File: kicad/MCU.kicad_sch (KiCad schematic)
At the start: 78 parts, among them J3 USART, J4 FAN, J5 USB_A, J6 Display, Q6 2N7002NXAK, Q7 2N7002K, Q8 2N7002K, SW1 ENC0 (Voltage), SW2 ENC1 (Current), SW3 BOOT, SW4 RST, U4 USBLC6-2SC6, U5 MCP9700A, U6 STM32F373C8Tx, Y1 Crystal

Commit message: Removed unnecessary stuff on fan tacho output
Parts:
- removed D7: SS16HE, Diode_SMD:D_SOD-323_HandSoldering, symbol Device:D_Schottky
- removed R30, R31, R35, R38: 10K, Resistor_SMD:R_0805_2012Metric_Pad1.20x1.40mm_HandSolder, symbol Device:R
- added C43: 100nF, symbol Device:C_Small
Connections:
- net GND: now also C43.2
- net at J4.3 (Pin_3), R34.2: now also C43.1
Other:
- moved on the sheet: R34

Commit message: Schematic work
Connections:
- net Iread: no longer U6.18 (PB0)
- net Iset: now also U6.16 (PA6); no longer U6.15 (PA5)
- net TEMP: now also U6.28 (PD8); no longer U6.14 (PA4)
- net Vread: no longer U6.19 (PB1)
- net Vset: now also U6.14 (PA4); no longer U6.16 (PA6)
- no-connect marks 8 -> 10

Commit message: Bunch of stuff
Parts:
- C42, C43: footprint (none) -> Capacitor_SMD:C_0805_2012Metric_Pad1.18x1.45mm_HandSolder
- J3: footprint (none) -> Connector_PinHeader_2.54mm:PinHeader_1x04_P2.54mm_Vertical
- JP1: value Jumper_2_Open -> 3V3 pullup on usb line; footprint (none) -> Jumper:SolderJumper-2_P1.3mm_Open_Pad1.0x1.5mm
- NT2, NT3, NT4, NT5: footprint (none) -> NetTie:NetTie-2_SMD_Pad0.5mm
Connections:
- net GNDA is gone; now on net GND: C18.1, C19.1, C20.1, C22.1, C23.1, C24.1, C28.1, C29.1, C30.1, U6.23 (VSSSD), U6.8 (VSSA)
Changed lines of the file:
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@@
 	)
 	(junction
+		(at 166.37 111.76)
+		(diameter 0)
+		(color 0 0 0 0)
+	)
+	(junction
 		(at 26.67 68.58)
 		(diameter 0)
@@
 	)
 	(junction
-		(at 171.45 111.76)
-		(diameter 0)
-		(color 0 0 0 0)
-	)
-	(junction
 		(at 26.67 26.67)
 		(diameter 0)
@@
 	)
 	(junction
+		(at 168.91 111.76)
+		(diameter 0)
+		(color 0 0 0 0)
+	)
+	(junction
 		(at 16.51 43.18)
 		(diameter 0)
@@
 	(wire
 		(pts
+			(xy 166.37 111.76) (xy 168.91 111.76)
+		)
+		(stroke
+			(width 0)
+			(type default)
+		)
+	)
+	(wire
+		(pts
 			(xy 158.75 134.62) (xy 163.83 134.62)
 		)
@@
 	(wire
 		(pts
-			(xy 171.45 111.76) (xy 173.99 111.76)
-		)
-		(stroke
-			(width 0)
-			(type default)
-		)
-	)
-	(wire
-		(pts
 			(xy 162.56 163.83) (xy 153.67 163.83)
 		)
@@
 	(wire
 		(pts
-			(xy 173.99 111.76) (xy 173.99 114.3)
-		)
-		(stroke
-			(width 0)
-			(type default)
-		)
-	)
-	(wire
-		(pts
 			(xy 166.37 27.94) (xy 168.91 27.94)
 		)
@@
 			)
 		)
-		(property "Footprint" ""
+		(property "Footprint" "Capacitor_SMD:C_0805_2012Metric_Pad1.18x1.45mm_HandSolder"
 			(at 158.75 138.43 0)
 			(effects
@@
 	)
 	(symbol
-		(lib_id "power:GNDA")
-		(at 173.99 114.3 0)
-		(unit 1)
-		(exclude_from_sim no)
-		(in_bom yes)
-		(on_board yes)
-		(dnp no)
-		(property "Reference" "#PWR068"
-			(at 173.99 120.65 0)
-			(effects
-				(font
-					(size 1.27 1.27)
-				)
-				(hide yes)
-			)
-		)
-		(property "Value" "GNDA"
-			(at 174.117 118.6942 0)
-			(effects
-				(font
-					(size 1.27 1.27)
-				)
-			)
-		)
-		(property "Footprint" ""
-			(at 173.99 114.3 0)
-			(effects
-				(font
-					(size 1.27 1.27)
-				)
-				(hide yes)
-			)
-		)
-		(property "Datasheet" ""
-			(at 173.99 114.3 0)
-			(effects
-				(font
-					(size 1.27 1.27)
-				)
-				(hide yes)
-			)
-		)
-		(property "Description" "Power symbol creates a global label with name \"GNDA\" , analog ground"
-			(at 173.99 114.3 0)
-			(effects
-				(font
-					(size 1.27 1.27)
-				)
-				(hide yes)
-			)
-		)
-		(pin "1"
-		)
-		(instances
-			(project ""
-				(path "/9538e4ed-27e6-4c37-b989-9859dc0d49e8/00000000-0000-0000-0000-00005f1751cc"
-					(reference "#PWR068")
-					(unit 1)
-				)
-			)
-		)
-	)
-	(symbol
 		(lib_id "Switch:SW_Push")
 		(at 113.03 40.64 0)
@@
 			)
 		)
-		(property "Value" "GNDA"
+		(property "Value" "GND"
 			(at 16.637 64.0842 0)
 			(effects
@@
 			)
 		)
-		(property "Value" "GNDA"
+		(property "Value" "GND"
 			(at 16.637 47.5742 0)
 			(effects
@@
 			)
 		)
-		(property "Value" "GNDA"
+		(property "Value" "GND"
 			(at 16.637 31.0642 0)
 			(effects
@@
 			)
 		)
-		(property "Footprint" ""
+		(property "Footprint" "Connector_PinHeader_2.54mm:PinHeader_1x04_P2.54mm_Vertical"
 			(at 29.21 90.17 0)
 			(effects
@@
 			)
 		)
-		(property "Value" "Jumper_2_Open"
+		(property "Value" "3V3 pullup on usb line"
 			(at 91.44 95.25 0)
 			(effects
@@
 			)
 		)
-		(property "Footprint" ""
+		(property "Footprint" "Jumper:SolderJumper-2_P1.3mm_Open_Pad1.0x1.5mm"
 			(at 91.44 99.06 0)
 			(effects
@@
 			)
 		)
-		(property "Footprint" ""
+		(property "Footprint" "NetTie:NetTie-2_SMD_Pad0.5mm"
 			(at 60.96 68.58 0)
 			(effects
@@
 			)
 		)
-		(property "Footprint" ""
+		(property "Footprint" "NetTie:NetTie-2_SMD_Pad0.5mm"
 			(at 52.07 21.59 0)
 			(effects
@@
 			)
 		)
-		(property "Footprint" ""
+		(property "Footprint" "NetTie:NetTie-2_SMD_Pad0.5mm"
 			(at 48.26 54.61 0)
 			(effects
@@
 			)
 		)
-		(property "Footprint" ""
+		(property "Footprint" "Capacitor_SMD:C_0805_2012Metric_Pad1.18x1.45mm_HandSolder"
 			(at 33.02 134.62 0)
 			(effects
@@
 			)
 		)
-		(property "Footprint" ""
+		(property "Footprint" "NetTie:NetTie-2_SMD_Pad0.5mm"
 			(at 52.07 38.1 0)
 			(effects

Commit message: Minor changes
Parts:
- removed C42: ?, Capacitor_SMD:C_0805_2012Metric_Pad1.18x1.45mm_HandSolder, symbol Device:C_Small
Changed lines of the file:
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@@
 	)
 	(junction
-		(at 158.75 134.62)
-		(diameter 0)
-		(color 0 0 0 0)
-	)
-	(junction
 		(at 26.67 59.69)
 		(diameter 0)
@@
 	(wire
 		(pts
-			(xy 158.75 142.24) (xy 158.75 140.97)
-		)
-		(stroke
-			(width 0)
-			(type default)
-		)
-	)
-	(wire
-		(pts
 			(xy 31.75 162.56) (xy 31.75 161.29)
 		)
@@
 	(wire
 		(pts
-			(xy 158.75 134.62) (xy 163.83 134.62)
+			(xy 156.21 134.62) (xy 163.83 134.62)
 		)
 		(stroke
@@
 	(wire
 		(pts
-			(xy 156.21 134.62) (xy 158.75 134.62)
-		)
-		(stroke
-			(width 0)
-			(type default)
-		)
-	)
-	(wire
-		(pts
 			(xy 162.56 163.83) (xy 153.67 163.83)
 		)
@@
 	(wire
 		(pts
-			(xy 158.75 134.62) (xy 158.75 135.89)
-		)
-		(stroke
-			(width 0)
-			(type default)
-		)
-	)
-	(wire
-		(pts
 			(xy 41.91 129.54) (xy 41.91 140.97)
 		)
@@
 	(wire
 		(pts
-			(xy 146.05 142.24) (xy 158.75 142.24)
-		)
-		(stroke
-			(width 0)
-			(type default)
-		)
-	)
-	(wire
-		(pts
 			(xy 115.57 179.07) (xy 120.65 179.07)
 		)
@@
 					(unit 1)
 				)
-			)
-		)
-	)
-	(symbol
-		(lib_id "Device:C_Small")
-		(at 158.75 138.43 0)
-		(unit 1)
-		(exclude_from_sim no)
-		(in_bom yes)
-		(on_board yes)
-		(dnp no)
-		(property "Reference" "C42"
-			(at 161.0868 137.2616 0)
-			(effects
-				(font
-					(size 1.27 1.27)
-				)
-				(justify left)
-			)
-		)
-		(property "Value" "?"
-			(at 161.0868 139.573 0)
-			(effects
-				(font
-					(size 1.27 1.27)
-				)
-				(justify left)
-			)
-		)
-		(property "Footprint" "Capacitor_SMD:C_0805_2012Metric_Pad1.18x1.45mm_HandSolder"
-			(at 158.75 138.43 0)
-			(effects
-				(font
-					(size 1.27 1.27)
-				)
-				(hide yes)
-			)
-		)
-		(property "Datasheet" "~"
-			(at 158.75 138.43 0)
-			(effects
-				(font
-					(size 1.27 1.27)
-				)
-				(hide yes)
-			)
-		)
-		(property "Description" "Unpolarized capacitor, small symbol"
-			(at 158.75 138.43 0)
-			(effects
-				(font
-					(size 1.27 1.27)
-				)
-				(hide yes)
-			)
-		)
-		(pin "1"
-		)
-		(pin "2"
-		)
-		(instances
-			(project ""
-				(path "/9538e4ed-27e6-4c37-b989-9859dc0d49e8/00000000-0000-0000-0000-00005f1751cc"
-					(reference "C42")
-					(unit 1)
-				)

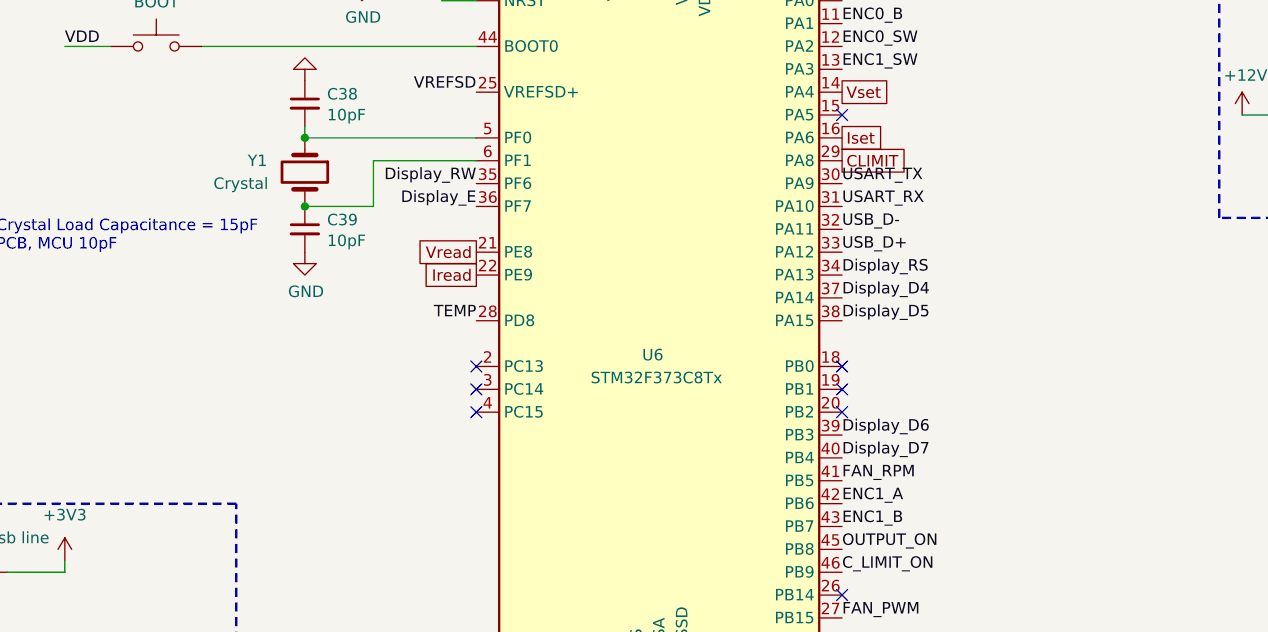
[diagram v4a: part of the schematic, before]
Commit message: Added series termination on display lines
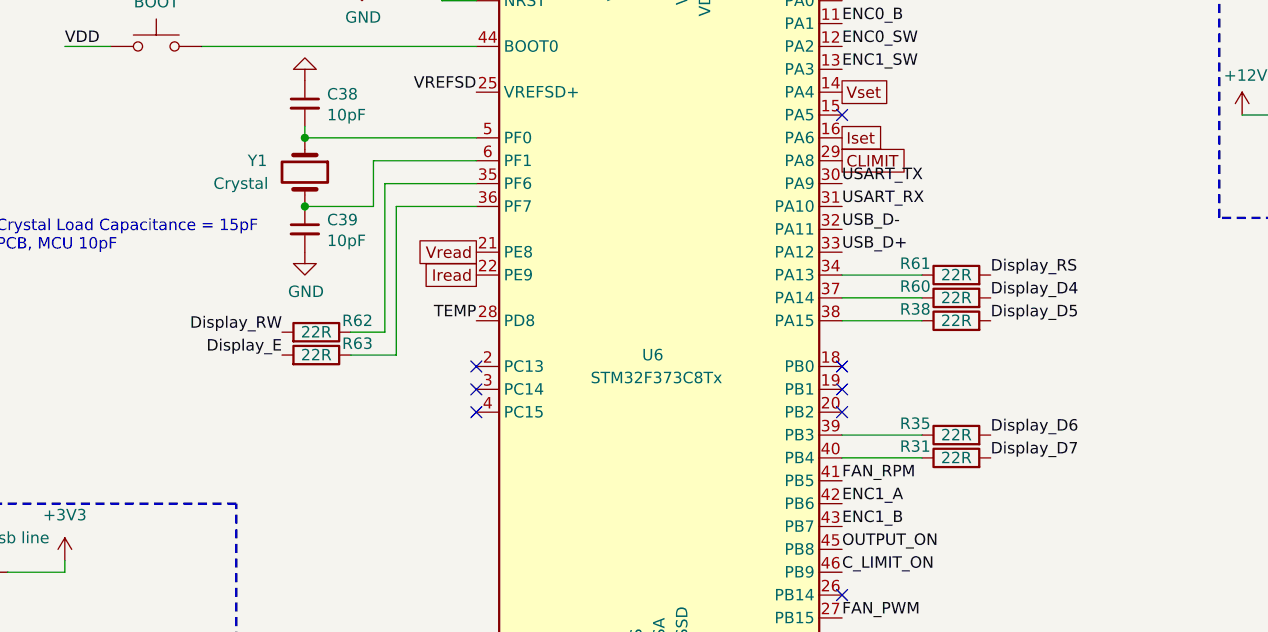
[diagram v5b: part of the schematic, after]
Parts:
- added R31, R35, R38, R60, R61, R62, R63: 22R, Resistor_SMD:R_0805_2012Metric_Pad1.20x1.40mm_HandSolder, symbol Device:R
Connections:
- net Display_D4: now also R60.2; no longer U6.37 (PA14)
- net Display_D5: now also R38.2; no longer U6.38 (PA15)
- net Display_D6: now also R35.2; no longer U6.39 (PB3)
- net Display_D7: now also R31.2; no longer U6.40 (PB4)
- net Display_E: now also R63.2; no longer U6.36 (PF7)
- net Display_RS: now also R61.2; no longer U6.34 (PA13)
- net Display_RW: now also R62.2; no longer U6.35 (PF6)
- new net: R61.1, U6.34 (PA13)
- new net: R62.1, U6.35 (PF6)
- new net: R63.1, U6.36 (PF7)
- new net: R60.1, U6.37 (PA14)
- new net: R38.1, U6.38 (PA15)
- new net: R35.1, U6.39 (PB3)
- new net: R31.1, U6.40 (PB4)

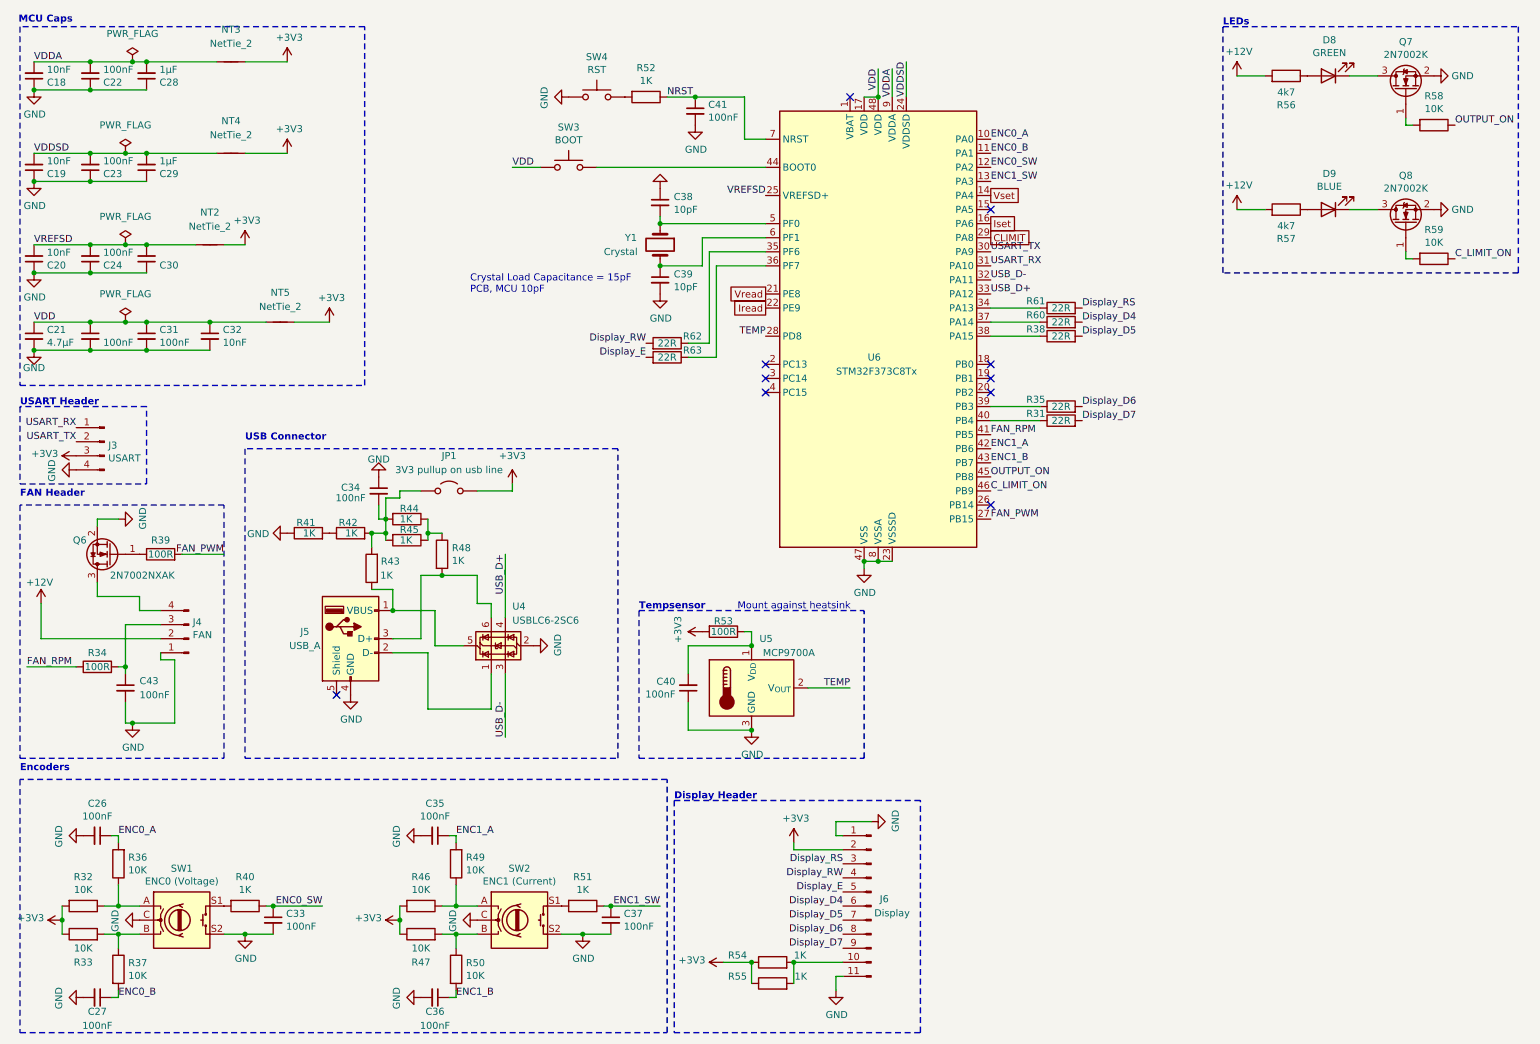
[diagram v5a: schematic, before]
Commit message: Changes and added Buck converter for 3V3
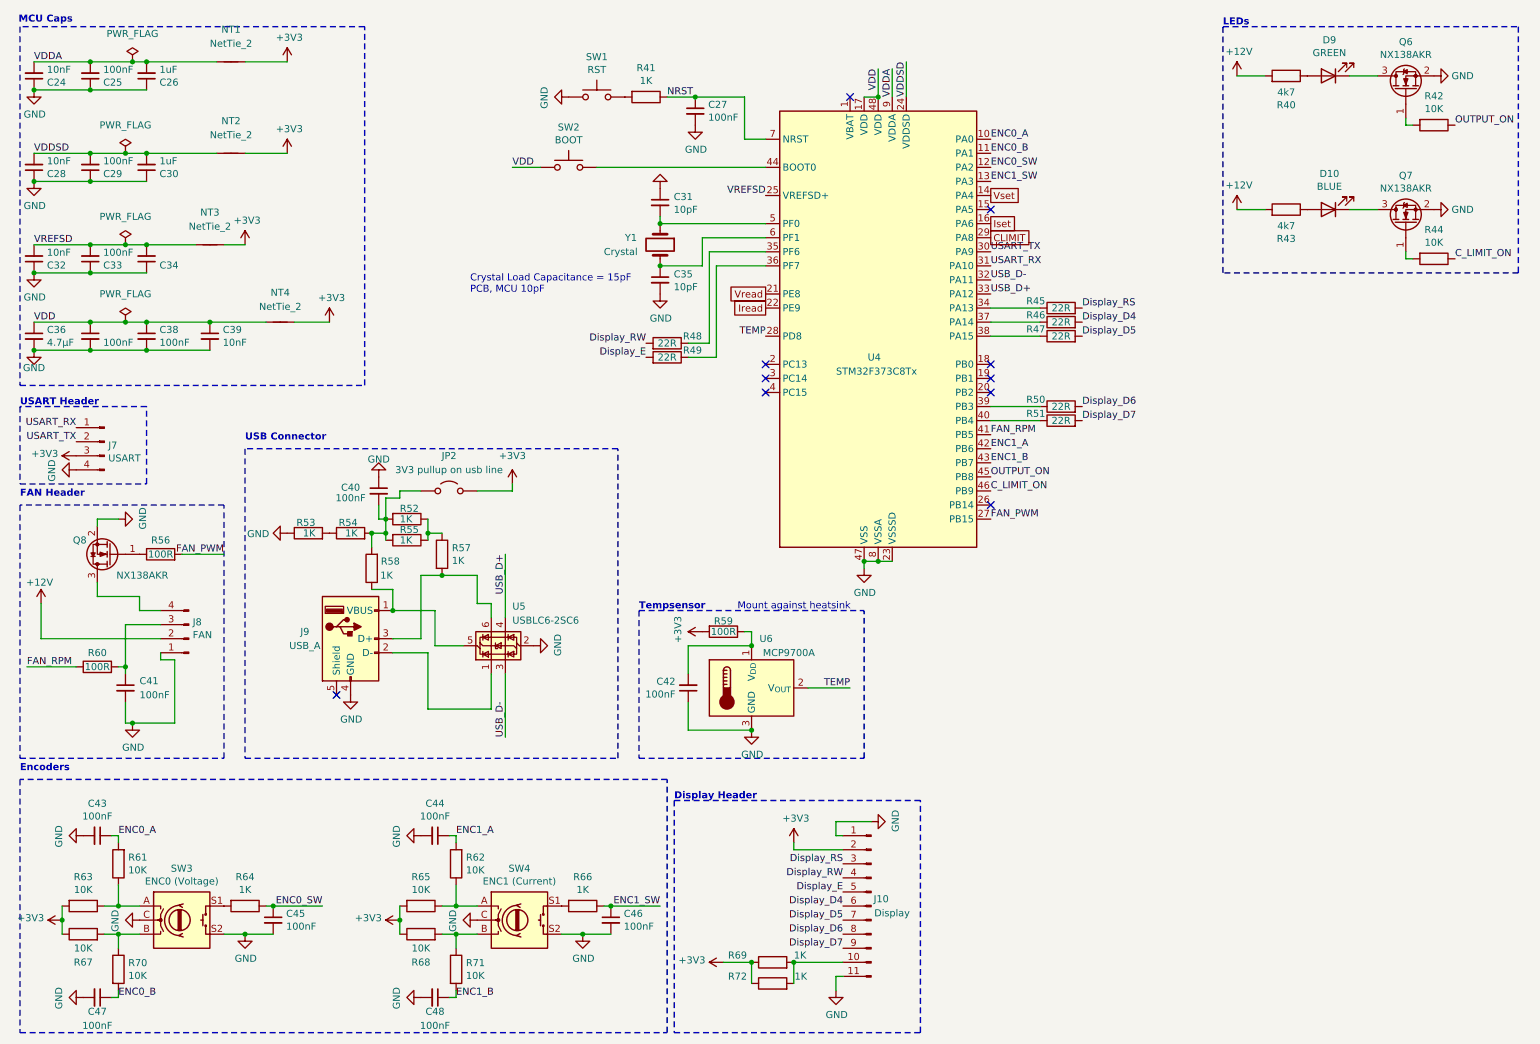
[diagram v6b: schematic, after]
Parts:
- C26: renamed from C28; value 1µF -> 1uF
- C27: renamed from C41; MPN CC0805KRX7R0BB103 -> CC0805KRX7R9BB104
- C30: renamed from C29; value 1µF -> 1uF
- C34: renamed from C30; value 1µF -> 1uF
- C36: renamed from C21; MPN GRM21BR71C475KE51L -> GRM21BR61H475ME51L
- C40: renamed from C34; MPN CC0805KRX7R0BB103 -> CC0805KRX7R9BB104
- C41: renamed from C43; MPN (none) -> CC0805KRX7R9BB104
- C42: renamed from C40; MPN CC0805KRX7R0BB103 -> CC0805KRX7R9BB104
- C43: renamed from C26; MPN CC0805KRX7R0BB103 -> CC0805KRX7R9BB104
- C44: renamed from C35; MPN CC0805KRX7R0BB103 -> CC0805KRX7R9BB104
- C45: renamed from C33; MPN CC0805KRX7R0BB103 -> CC0805KRX7R9BB104
- C46: renamed from C37; MPN CC0805KRX7R0BB103 -> CC0805KRX7R9BB104
- C47: renamed from C27; MPN CC0805KRX7R0BB103 -> CC0805KRX7R9BB104
- C48: renamed from C36; MPN CC0805KRX7R0BB103 -> CC0805KRX7R9BB104
- Q6: renamed from Q7; value 2N7002K -> NX138AKR; footprint Package_TO_SOT_SMD:SOT-23 -> Package_TO_SOT_SMD:SOT-23-3; MPN (none) -> NX138AKR
- Q7: renamed from Q8; value 2N7002K -> NX138AKR; footprint Package_TO_SOT_SMD:SOT-23 -> Package_TO_SOT_SMD:SOT-23-3; MPN (none) -> NX138AKR
- Q8: renamed from Q6; value 2N7002NXAK -> NX138AKR; footprint Package_TO_SOT_SMD:SOT-23 -> Package_TO_SOT_SMD:SOT-23-3; MPN 2N7002NXAK -> NX138AKR
- R42: renamed from R58; MPN CRCW080510K0FKEAC -> RC0805FR-1310KL
- R44: renamed from R59; MPN CRCW080510K0FKEAC -> RC0805FR-1310KL
- R61: renamed from R36; MPN CRCW080510K0FKEAC -> RC0805FR-1310KL
- R62: renamed from R49; MPN CRCW080510K0FKEAC -> RC0805FR-1310KL
- R63: renamed from R32; MPN CRCW080510K0FKEAC -> RC0805FR-1310KL
- R65: renamed from R46; MPN CRCW080510K0FKEAC -> RC0805FR-1310KL
- R67: renamed from R33; MPN CRCW080510K0FKEAC -> RC0805FR-1310KL
- R68: renamed from R47; MPN CRCW080510K0FKEAC -> RC0805FR-1310KL
- R70: renamed from R37; MPN CRCW080510K0FKEAC -> RC0805FR-1310KL
- R71: renamed from R50; MPN CRCW080510K0FKEAC -> RC0805FR-1310KL
- U4: renamed from U6; MPN (none) -> STM32F373C8Tx
- renumbered C18 to C24, C22 to C25, C19 to C28, C23 to C29, C38 to C31, C20 to C32, C24 to C33, C39 to C35, C25 to C37, C31 to C38, C32 to C39, D9 to D10, D8 to D9, J6 to J10, J3 to J7, J4 to J8, J5 to J9, JP1 to JP2, NT3 to NT1, NT4 to NT2, NT2 to NT3, NT5 to NT4, R56 to R40, R52 to R41, R57 to R43, R61 to R45, R60 to R46, R38 to R47, R62 to R48, R63 to R49, R35 to R50, R31 to R51, R44 to R52, R41 to R53, R42 to R54, R45 to R55, R39 to R56, R48 to R57, R43 to R58, R53 to R59, R34 to R60, R40 to R64, R51 to R66, R54 to R69, R55 to R72, SW4 to SW1, SW3 to SW2, SW1 to SW3, SW2 to SW4, U4 to U5, U5 to U6
